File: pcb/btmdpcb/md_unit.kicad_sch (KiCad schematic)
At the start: 15 parts, among them J3 Conn_01x03_Pin, J4 Conn_01x02_Pin, SW1 SW_SPST, SW2 SW_Push, SW3 SW_SPST

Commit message: Clean up schematic, implement all logic functionality
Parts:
- renumbered J4 to J3, J3 to J4, R31 to R30, R17 to R31, R30 to R32, SW3 to SW1, SW1 to SW3, TP12 to TP10, TP5 to TP11, TP11 to TP12, TP4 to TP13, TP13 to TP7, TP6 to TP8, TP3 to TP9
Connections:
- net 1V5in renamed 1V5_IN
- net PWR_EN renamed DVDD_OUT
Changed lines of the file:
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@@
+	)
+	(junction
+		(at 107.95 59.69)
+		(diameter 0)
+		(color 0 0 0 0)
 	)
 	(junction
@@
 	(wire
 		(pts
+			(xy 107.95 59.69) (xy 114.3 59.69)
+		)
+		(stroke
+			(width 0)
+			(type default)
+		)
+	)
+	(wire
+		(pts
 			(xy 100.33 36.83) (xy 101.6 36.83)
 		)
@@
 	(wire
 		(pts
-			(xy 87.63 59.69) (xy 99.06 59.69)
+			(xy 87.63 59.69) (xy 107.95 59.69)
 		)
 		(stroke
@@
 		)
 	)
-	(hierarchical_label "PWR_EN"
+	(hierarchical_label "DVDD_OUT"
 		(shape output)
-		(at 99.06 59.69 0)
+		(at 114.3 59.69 0)
 		(fields_autoplaced yes)
 		(effects
@@
 		)
 		(property "Function" "Keep 1.5V source alive after button is released"
-			(at 99.06 60.96 0)
+			(at 114.3 60.96 0)
 			(effects
 				(font
@@
 		)
 		(property "Level" "2.2V"
-			(at 99.06 62.611 0)
+			(at 114.3 62.611 0)
 			(effects
 				(font
@@
 			)
 		)
-		(property "Location" "TODO: location on MZ-N505"
-			(at 99.06 64.262 0)
-			(effects
-				(font
-					(size 1.27 1.27)
-					(italic yes)
-				)
-				(justify left)
-			)
-		)
-	)
-	(hierarchical_label "BTN_PLAY"
+	)
+	(hierarchical_label "AUDIO_R"
 		(shape output)
-		(at 116.84 173.99 0)
+		(at 111.76 39.37 0)
 		(fields_autoplaced yes)
 		(effects
@@
 			(justify left)
 		)
-		(property "Function" "Bootstrap power by enabling 1.5V regulator"
-			(at 116.84 175.26 0)
-			(effects
-				(font
-					(size 1.27 1.27)
-					(italic yes)
-				)
-				(justify left)
-			)
-		)
-		(property "Level" "???"
-			(at 116.84 176.911 0)
-			(effects
-				(font
-					(size 1.27 1.27)
-					(italic yes)
-				)
-				(justify left)
-			)
-		)
-		(property "Location" "TODO: location on MZ-N505"
-			(at 116.84 178.562 0)
-			(effects
-				(font
-					(size 1.27 1.27)
-					(italic yes)
-				)
-				(justify left)
-			)
-		)
-	)
-	(hierarchical_label "AUDIO_R"
-		(shape output)
-		(at 111.76 39.37 0)
+	)
+	(hierarchical_label "GND"
+		(shape passive)
+		(at 111.76 97.79 270)
 		(fields_autoplaced yes)
 		(effects
@@
 				(size 1.27 1.27)
 			)
-			(justify left)
-		)
-	)
-	(hierarchical_label "GND"
-		(shape passive)
-		(at 111.76 97.79 270)
+			(justify right)
+		)
+	)
+	(hierarchical_label "~{BTN_PAUSE}_OUT"
+		(shape output)
+		(at 116.84 142.24 0)
 		(fields_autoplaced yes)
 		(effects
@@
 				(size 1.27 1.27)
 			)
-			(justify right)
-		)
-	)
-	(hierarchical_label "~{BTN_PAUSE}_OUT"
-		(shape output)
-		(at 116.84 142.24 0)
-		(fields_autoplaced yes)
-		(effects
-			(font
-				(size 1.27 1.27)
-			)
 			(justify left)
 		)
 	)
-	(hierarchical_label "1V5in"
+	(hierarchical_label "1V5_IN"
 		(shape input)
 		(at 35.56 39.37 180)
@@
 		(dnp yes)
 		(fields_autoplaced yes)
-		(property "Reference" "R31"
+		(property "Reference" "R30"
 			(at 93.98 135.89 90)
 			(effects
@@
 			(project "btmdpcb"
 				(path "/6e43e92f-e106-411c-86ee-217d084aee5b/e9a1d5eb-4561-44c0-9558-fc81dabbe286"
-					(reference "R31")
+					(reference "R30")
 					(unit 1)
 				)
@@
 		(dnp yes)
 		(fields_autoplaced yes)
-		(property "Reference" "R17"
+		(property "Reference" "R31"
 			(at 97.79 101.6 90)
 			(effects
@@
 			(project ""
 				(path "/6e43e92f-e106-411c-86ee-217d084aee5b/e9a1d5eb-4561-44c0-9558-fc81dabbe286"
-					(reference "R17")
+					(reference "R31")
 					(unit 1)
 				)
@@
 		(dnp no)
 		(fields_autoplaced yes)
-		(property "Reference" "J4"
+		(property "Reference" "J3"
 			(at 50.8 39.3699 0)
 			(effects
@@
 			(project ""
 				(path "/6e43e92f-e106-411c-86ee-217d084aee5b/e9a1d5eb-4561-44c0-9558-fc81dabbe286"
-					(reference "J4")
+					(reference "J3")
 					(unit 1)
 				)
@@
 		(dnp no)
 		(fields_autoplaced yes)
-		(property "Reference" "TP4"
+		(property "Reference" "TP13"
 			(at 127 103.3779 0)
 			(effects
@@
 			(project "btmdpcb"
 				(path "/6e43e92f-e106-411c-86ee-217d084aee5b/e9a1d5eb-4561-44c0-9558-fc81dabbe286"
-					(reference "TP4")
+					(reference "TP13")
 					(unit 1)
 				)
@@
 		(dnp no)
 		(fields_autoplaced yes)
-		(property "Reference" "SW1"
+		(property "Reference" "SW3"
 			(at 113.03 111.7599 90)
 			(effects
@@
 			(project ""
 				(path "/6e43e92f-e106-411c-86ee-217d084aee5b/e9a1d5eb-4561-44c0-9558-fc81dabbe286"
-					(reference "SW1")
+					(reference "SW3")
 					(unit 1)
 				)
@@
 		(dnp no)
 		(fields_autoplaced yes)
-		(property "Reference" "TP11"
+		(property "Reference" "TP12"
 			(at 116.84 77.9779 0)
 			(effects
@@
 			(project "btmdpcb"
 				(path "/6e43e92f-e106-411c-86ee-217d084aee5b/e9a1d5eb-4561-44c0-9558-fc81dabbe286"
-					(reference "TP11")
+					(reference "TP12")
 					(unit 1)
 				)
@@
 		(dnp yes)
 		(fields_autoplaced yes)
-		(property "Reference" "R30"
+		(property "Reference" "R32"
 			(at 104.14 76.2 90)
 			(effects
@@
 			(project "btmdpcb"
 				(path "/6e43e92f-e106-411c-86ee-217d084aee5b/e9a1d5eb-4561-44c0-9558-fc81dabbe286"
-					(reference "R30")
+					(reference "R32")
 					(unit 1)
 				)
@@
 		(dnp no)
 		(fields_autoplaced yes)
-		(property "Reference" "TP12"
+		(property "Reference" "TP10"
 			(at 90.17 76.7079 0)
 			(effects
@@
 			(project "btmdpcb"
 				(path "/6e43e92f-e106-411c-86ee-217d084aee5b/e9a1d5eb-4561-44c0-9558-fc81dabbe286"
-					(reference "TP12")
+					(reference "TP10")
+					(unit 1)
+				)
+			)
+		)
+	)
+	(symbol
+		(lib_id "power:PWR_FLAG")
+		(at 107.95 59.69 0)
+		(unit 1)
+		(exclude_from_sim no)
+		(in_bom yes)
+		(on_board yes)
+		(dnp no)
+		(fields_autoplaced yes)
+		(property "Reference" "#FLG08"
+			(at 107.95 57.785 0)
+			(effects
+				(font
+					(size 1.27 1.27)
+				)
+				(hide yes)
+			)
+		)
+		(property "Value" "PWR_FLAG"
+			(at 107.95 54.61 0)
+			(effects
+				(font
+					(size 1.27 1.27)
+				)
+			)
+		)
+		(property "Footprint" ""
+			(at 107.95 59.69 0)
+			(effects
+				(font
+					(size 1.27 1.27)
+				)
+				(hide yes)
+			)
+		)
+		(property "Datasheet" "~"
+			(at 107.95 59.69 0)
+			(effects
+				(font
+					(size 1.27 1.27)
+				)
+				(hide yes)
+			)
+		)
+		(property "Description" "Special symbol for telling ERC where power comes from"
+			(at 107.95 59.69 0)
+			(effects
+				(font
+					(size 1.27 1.27)
+				)
+				(hide yes)
+			)
+		)
+		(pin "1"
+		)
+		(instances
+			(project ""
+				(path "/6e43e92f-e106-411c-86ee-217d084aee5b/e9a1d5eb-4561-44c0-9558-fc81dabbe286"
+					(reference "#FLG08")
 					(unit 1)
 				)
@@
 		(dnp no)
 		(fields_autoplaced yes)
-		(property "Reference" "TP3"
+		(property "Reference" "TP9"
 			(at 90.17 55.1179 0)
 			(effects
@@
 			(project "btmdpcb"
 				(path "/6e43e92f-e106-411c-86ee-217d084aee5b/e9a1d5eb-4561-44c0-9558-fc81dabbe286"
-					(reference "TP3")
+					(reference "TP9")
 					(unit 1)
 				)
@@
 		(dnp no)
 		(fields_autoplaced yes)
-		(property "Reference" "SW3"
+		(property "Reference" "SW1"
 			(at 104.14 148.5899 90)
 			(effects
@@
 			(project "btmdpcb"
 				(path "/6e43e92f-e106-411c-86ee-217d084aee5b/e9a1d5eb-4561-44c0-9558-fc81dabbe286"
-					(reference "SW3")
+					(reference "SW1")
 					(unit 1)
 				)
@@
 		(on_board yes)
 		(dnp no)
-		(property "Reference" "J3"
+		(property "Reference" "J4"
 			(at 95.885 31.75 0)
 			(effects
@@
 			(project ""
 				(path "/6e43e92f-e106-411c-86ee-217d084aee5b/e9a1d5eb-4561-44c0-9558-fc81dabbe286"
-					(reference "J3")
+					(reference "J4")
 					(unit 1)
 				)
@@
 		(dnp no)
 		(fields_autoplaced yes)
-		(property "Reference" "TP5"
+		(property "Reference" "TP11"
 			(at 107.95 137.6679 0)
 			(effects
@@
 			(project "btmdpcb"
 				(path "/6e43e92f-e106-411c-86ee-217d084aee5b/e9a1d5eb-4561-44c0-9558-fc81dabbe286"
-					(reference "TP5")
+					(reference "TP11")
 					(unit 1)
 				)
@@
 		(dnp no)
 		(fields_autoplaced yes)
-		(property "Reference" "TP13"
+		(property "Reference" "TP7"
 			(at 81.28 136.3979 0)
 			(effects
@@
 			(project "btmdpcb"
 				(path "/6e43e92f-e106-411c-86ee-217d084aee5b/e9a1d5eb-4561-44c0-9558-fc81dabbe286"
-					(reference "TP13")
+					(reference "TP7")
 					(unit 1)
 				)
@@
 		(dnp no)
 		(fields_autoplaced yes)
-		(property "Reference" "TP6"
+		(property "Reference" "TP8"
 			(at 82.55 100.8379 0)
 			(effects
@@
 			(project "btmdpcb"
 				(path "/6e43e92f-e106-411c-86ee-217d084aee5b/e9a1d5eb-4561-44c0-9558-fc81dabbe286"
-					(reference "TP6")
+					(reference "TP8")
 					(unit 1)
 				)

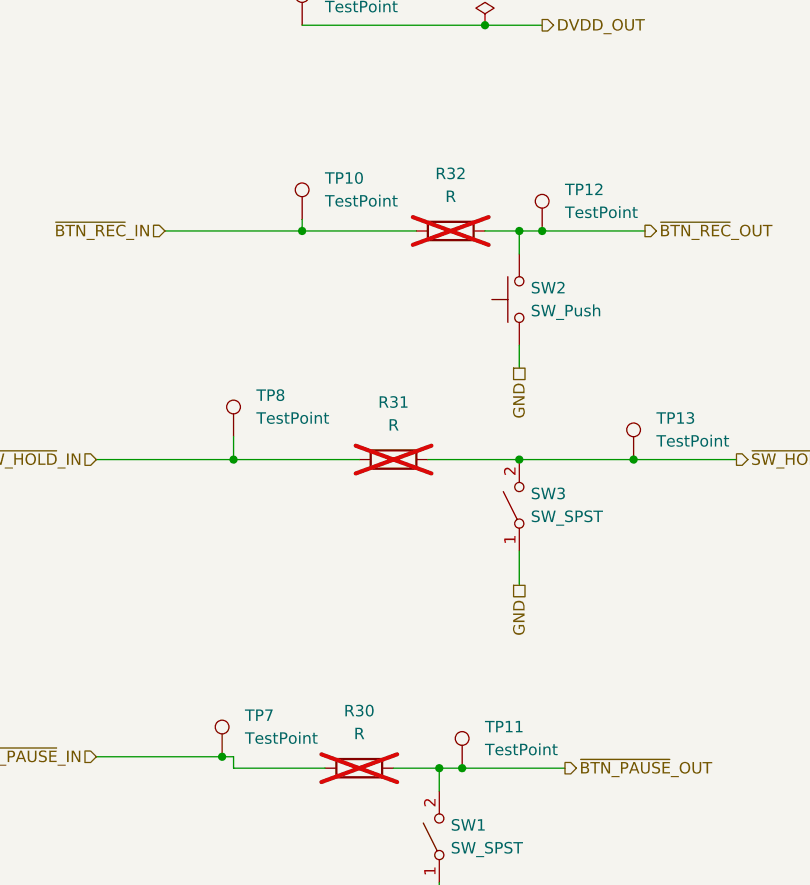
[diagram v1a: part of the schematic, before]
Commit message: Remove redundant regulators, simplify schematic
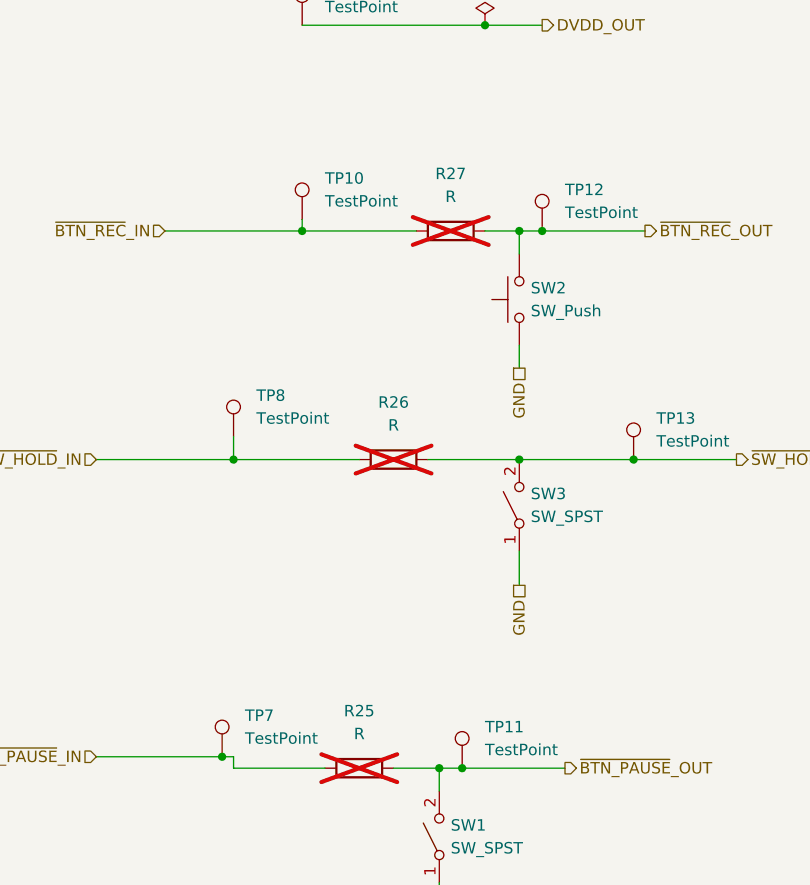
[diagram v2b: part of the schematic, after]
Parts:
- renumbered R30 to R25, R31 to R26, R32 to R27
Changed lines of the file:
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@@
 		(dnp yes)
 		(fields_autoplaced yes)
-		(property "Reference" "R30"
+		(property "Reference" "R25"
 			(at 93.98 135.89 90)
 			(effects
@@
 			(project "btmdpcb"
 				(path "/6e43e92f-e106-411c-86ee-217d084aee5b/e9a1d5eb-4561-44c0-9558-fc81dabbe286"
-					(reference "R30")
+					(reference "R25")
 					(unit 1)
 				)
@@
 		(dnp yes)
 		(fields_autoplaced yes)
-		(property "Reference" "R31"
+		(property "Reference" "R26"
 			(at 97.79 101.6 90)
 			(effects
@@
 			(project ""
 				(path "/6e43e92f-e106-411c-86ee-217d084aee5b/e9a1d5eb-4561-44c0-9558-fc81dabbe286"
-					(reference "R31")
+					(reference "R26")
 					(unit 1)
 				)
@@
 		(dnp yes)
 		(fields_autoplaced yes)
-		(property "Reference" "R32"
+		(property "Reference" "R27"
 			(at 104.14 76.2 90)
 			(effects
@@
 			(project "btmdpcb"
 				(path "/6e43e92f-e106-411c-86ee-217d084aee5b/e9a1d5eb-4561-44c0-9558-fc81dabbe286"
-					(reference "R32")
+					(reference "R27")
 					(unit 1)
 				)
@@
 		(dnp no)
 		(fields_autoplaced yes)
-		(property "Reference" "#FLG08"
+		(property "Reference" "#FLG06"
 			(at 107.95 57.785 0)
 			(effects
@@
 			(project ""
 				(path "/6e43e92f-e106-411c-86ee-217d084aee5b/e9a1d5eb-4561-44c0-9558-fc81dabbe286"
-					(reference "#FLG08")
-					(unit 1)
-				)
+					(reference "#FLG06")
+					(unit 1)
+				)

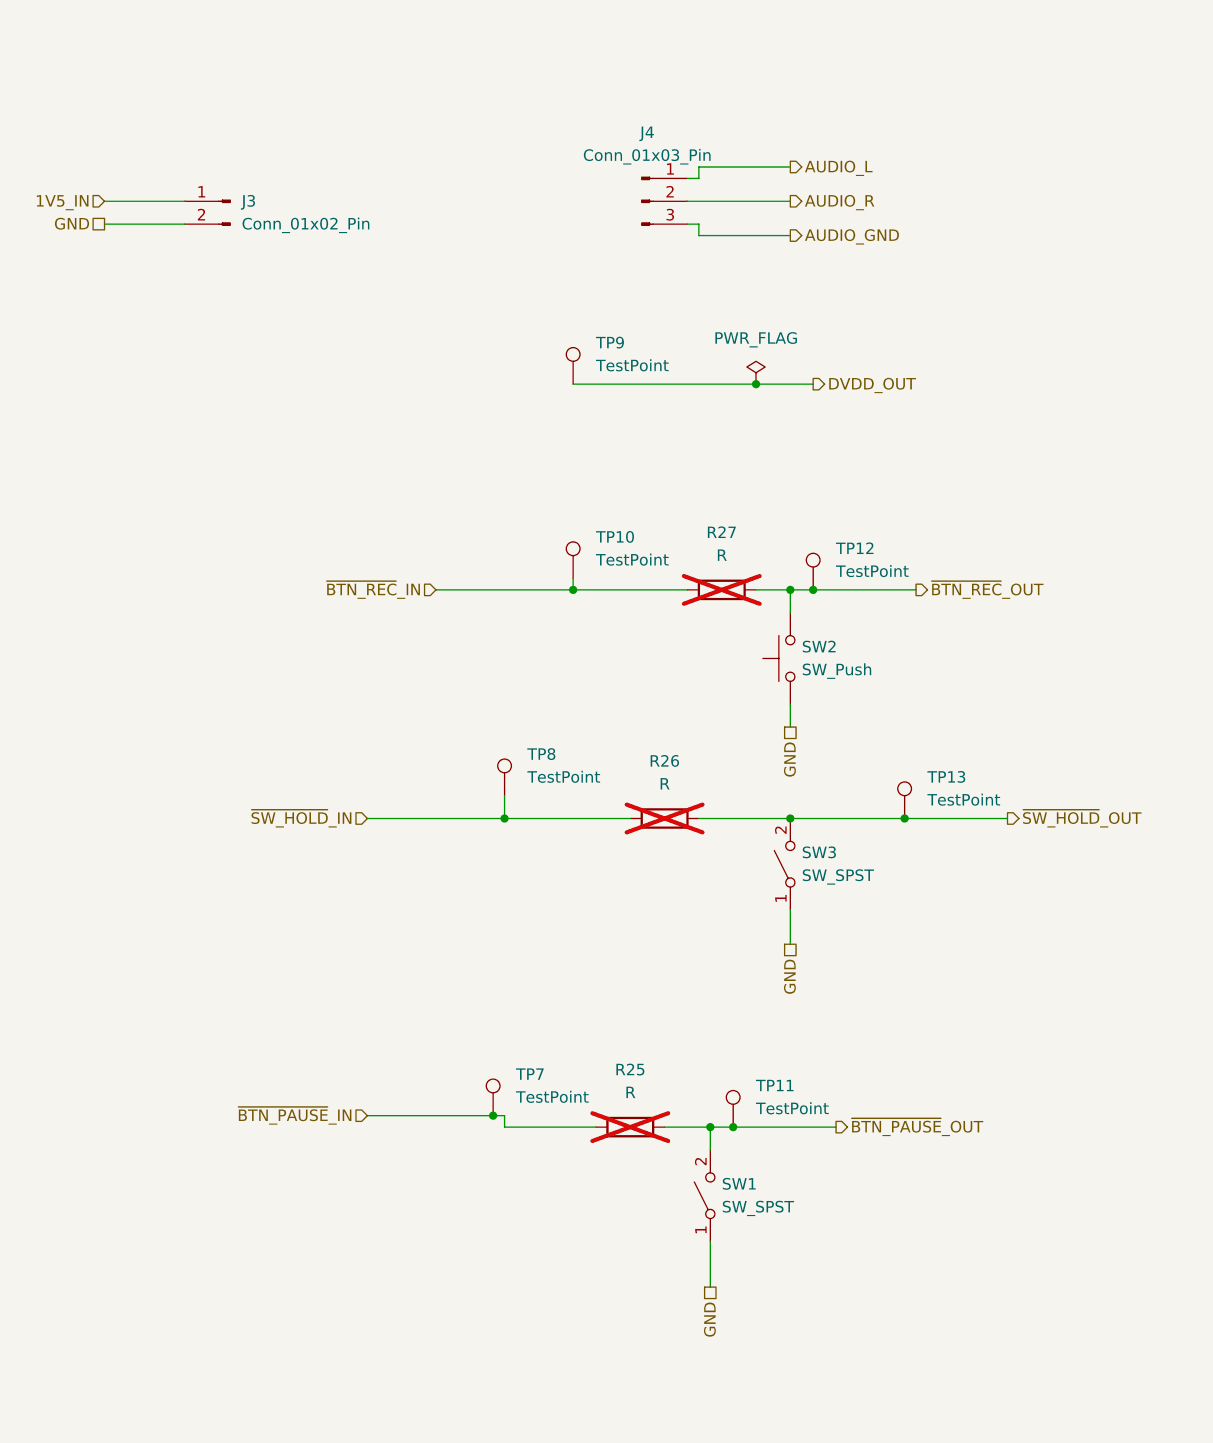
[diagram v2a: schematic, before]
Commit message: Add missing libraries, assign all footprints
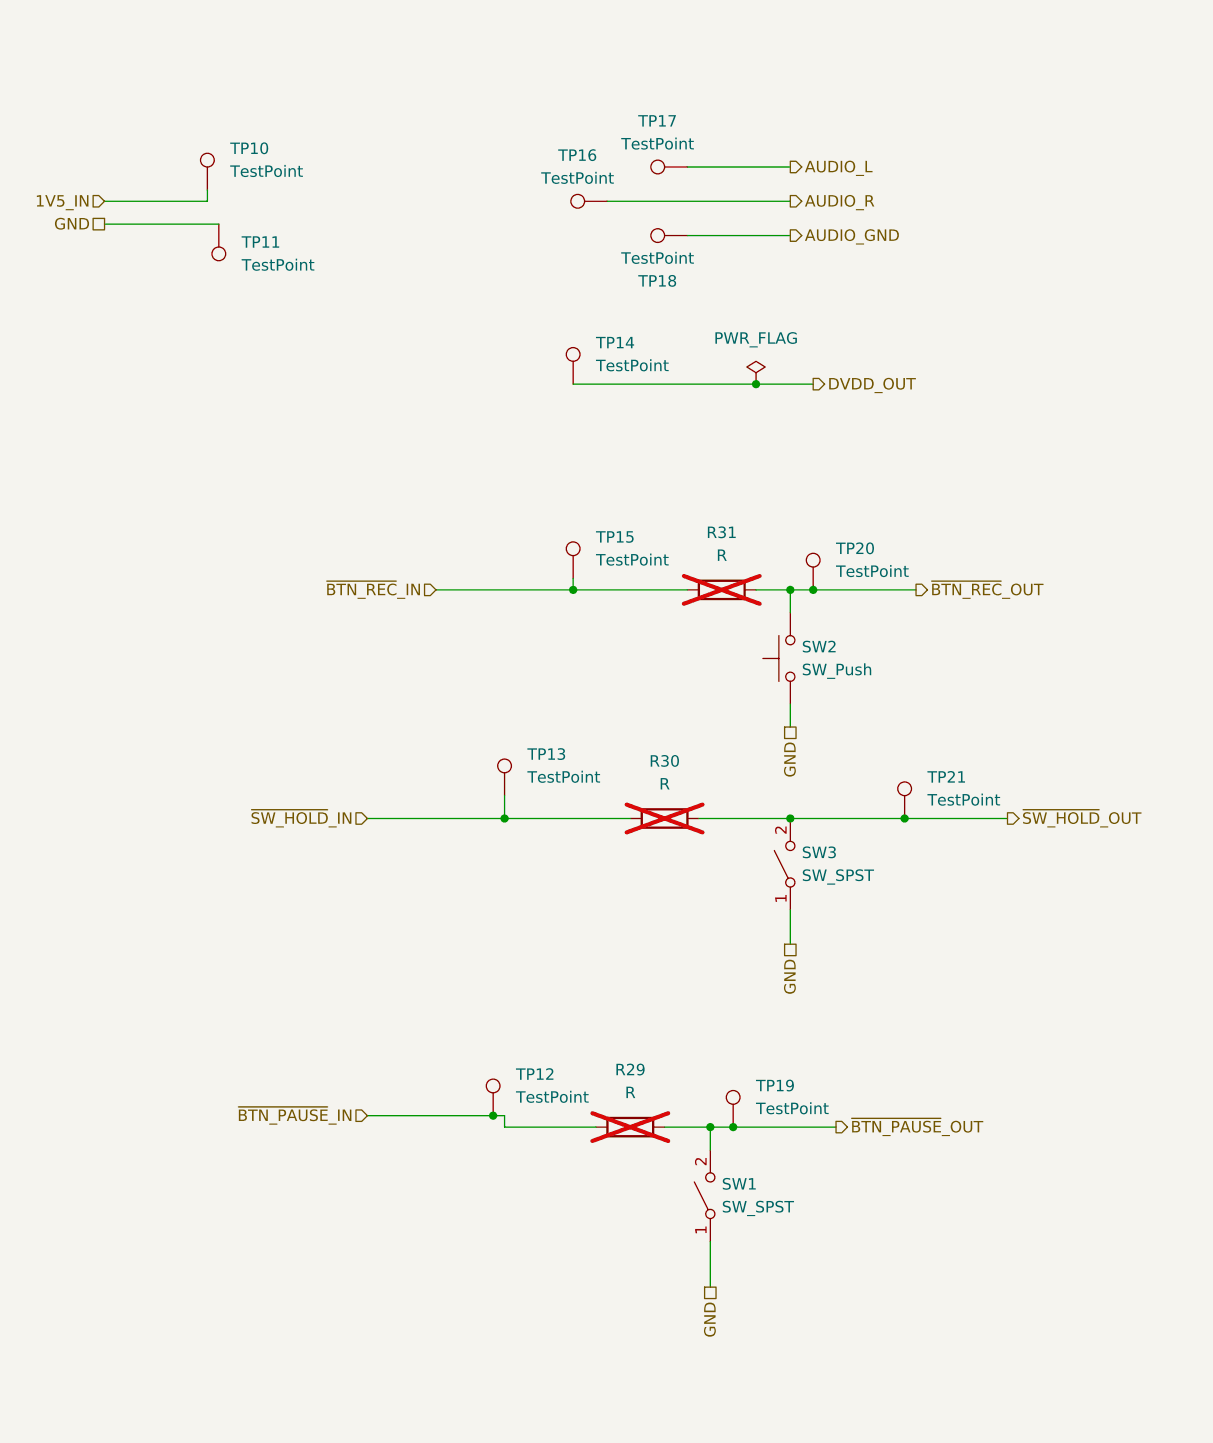
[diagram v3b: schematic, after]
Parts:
- removed J3: Conn_01x02_Pin, symbol Connector:Conn_01x02_Pin
- removed J4: Conn_01x03_Pin, symbol Connector:Conn_01x03_Pin
- added TP10, TP11, TP16, TP17, TP18: TestPoint, TestPoint:TestPoint_Pad_D1.0mm, symbol Connector:TestPoint
- renumbered R25 to R29, R26 to R30, R27 to R31, TP7 to TP12, TP8 to TP13, TP9 to TP14, TP10 to TP15, TP11 to TP19, TP12 to TP20, TP13 to TP21
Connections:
- net 1V5_IN: now also TP10.1
- net AUDIO_GND: now also TP18.1
- net AUDIO_L: now also TP17.1
- net AUDIO_R: now also TP16.1
- net GND: now also TP11.1

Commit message: Layout PCB
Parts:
- removed R29: R, symbol Device:R
- removed SW1: SW_SPST, symbol Switch:SW_SPST
- removed TP12, TP19: TestPoint, TestPoint:TestPoint_Pad_D1.0mm, symbol Connector:TestPoint
- TP12: renamed from TP10; value TestPoint -> 1V5
- TP13: renamed from TP11; value TestPoint -> GND
- TP14: renamed from TP15; value TestPoint -> MD_BTN_REC_IN; now not fitted
- TP15: renamed from TP13; value TestPoint -> HOLD
- TP16: renamed from TP17; value TestPoint -> L
- TP17: renamed from TP16; value TestPoint -> R
- TP18: value TestPoint -> AGND
- TP19: renamed from TP14; value TestPoint -> DVDD
- TP20: value TestPoint -> REC
- TP21: value TestPoint -> HOLD
- renumbered R31 to R23, R30 to R24, SW2 to SW1, SW3 to SW2
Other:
- moved on the sheet: R24, TP13, TP15, TP16, TP17, TP19, TP20, TP21
